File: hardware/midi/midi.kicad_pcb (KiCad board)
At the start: 2 copper layers, 100 x 62 mm, 52 parts, among them J2 Midi Out, J4 Power, J6 MIDI In, J7 USB_A, J8 I2C0, J9 I2C1, Q1 BSS138, Q3 TSM680P06, Q4 BSS138, SW1 Reset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

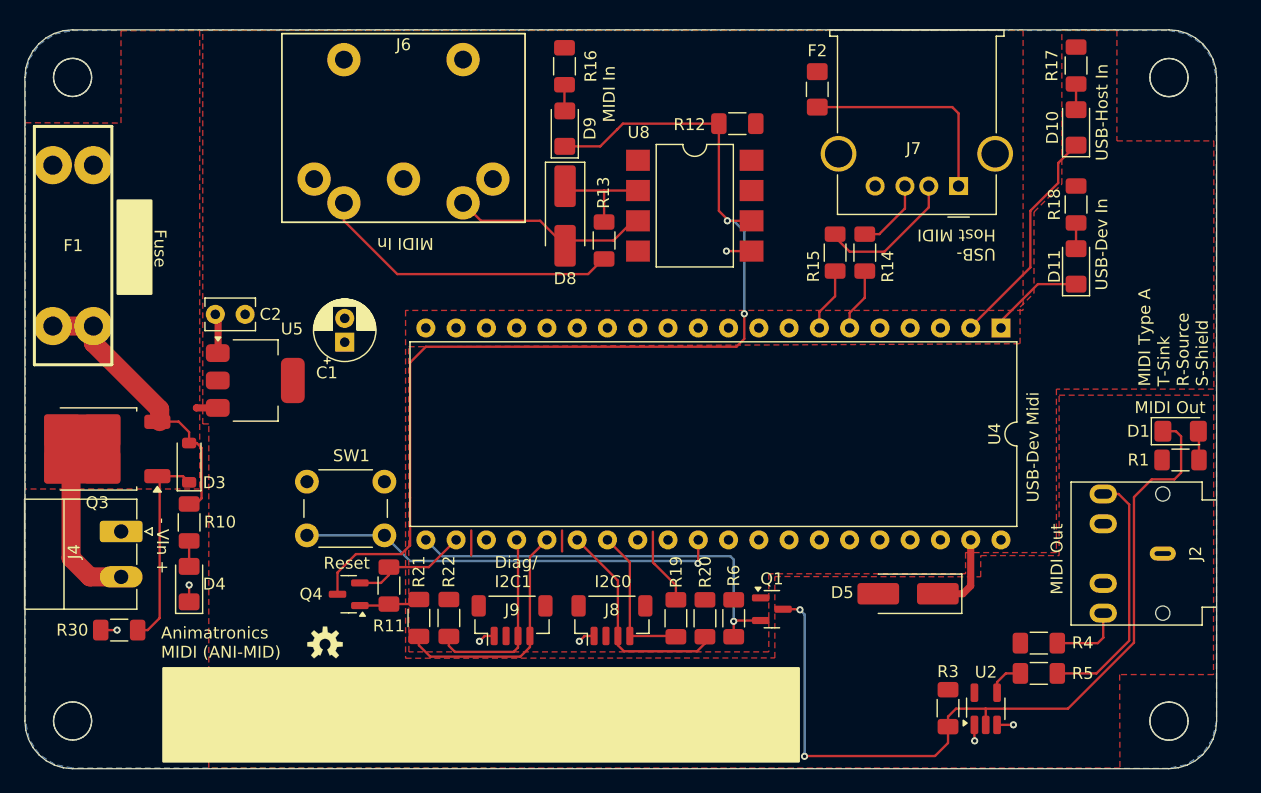
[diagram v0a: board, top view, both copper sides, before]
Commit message: Rev 1.1: - Update to latest KiCad - Fixed short in servo board - Updates to right-angle diag connector on servo boards - Fixed microproc footprint on diag board - Flipped I2C connector to top of diag board - Pass all ERC and DRC checks, add exclusions
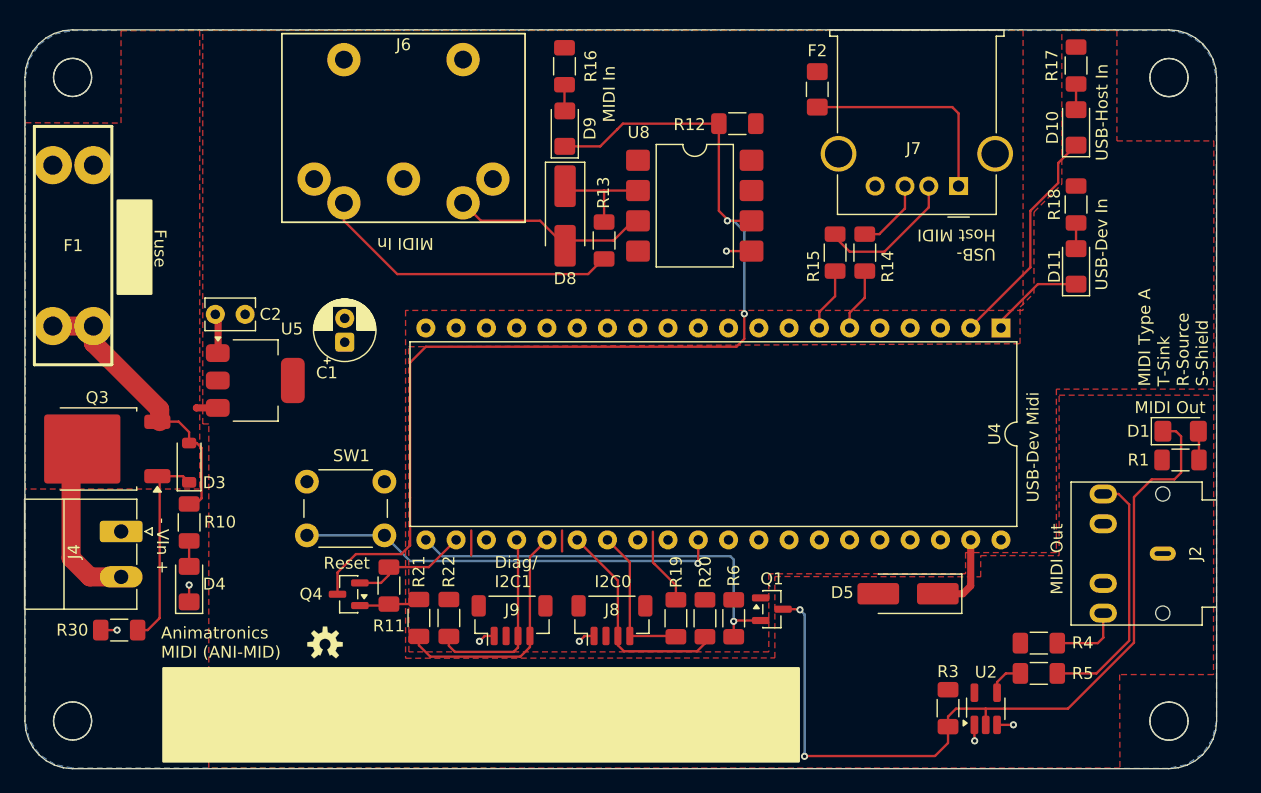
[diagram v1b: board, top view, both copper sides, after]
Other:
- board text added: "ANI-MID, Rev 1.1 Sparky Bobo Designs"
- board text removed: "ANI-MID, Rev 1.0 Sparky Bobo Designs"
